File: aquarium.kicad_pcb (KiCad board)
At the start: 2 copper layers, 104 x 47 mm, 40 parts, among them U1 MOC3063, U2 MOC3063

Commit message: ATmega48PA changet to ATmega8A
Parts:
- DD4: value ATMEGA48PA -> ATMEGA8A
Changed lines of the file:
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@@
     (links 93)
     (no_connects 2)
-    (area 74.899999 67.875 220.208334 135.300002)
+    (area 92.924999 82.924999 197.075001 130.075001)
     (thickness 1.6)
     (drawings 50)
@@
       (effects (font (size 1 1) (thickness 0.15)))
     )
-    (fp_text value ATMEGA48PA (at 0 0 90) (layer F.SilkS) hide
-      (effects (font (size 1 1) (thickness 0.15)))
-    )
+    (fp_text value ATMEGA8A (at 0 0 90) (layer F.SilkS) hide
+      (effects (font (size 1 1) (thickness 0.15)))
+    )

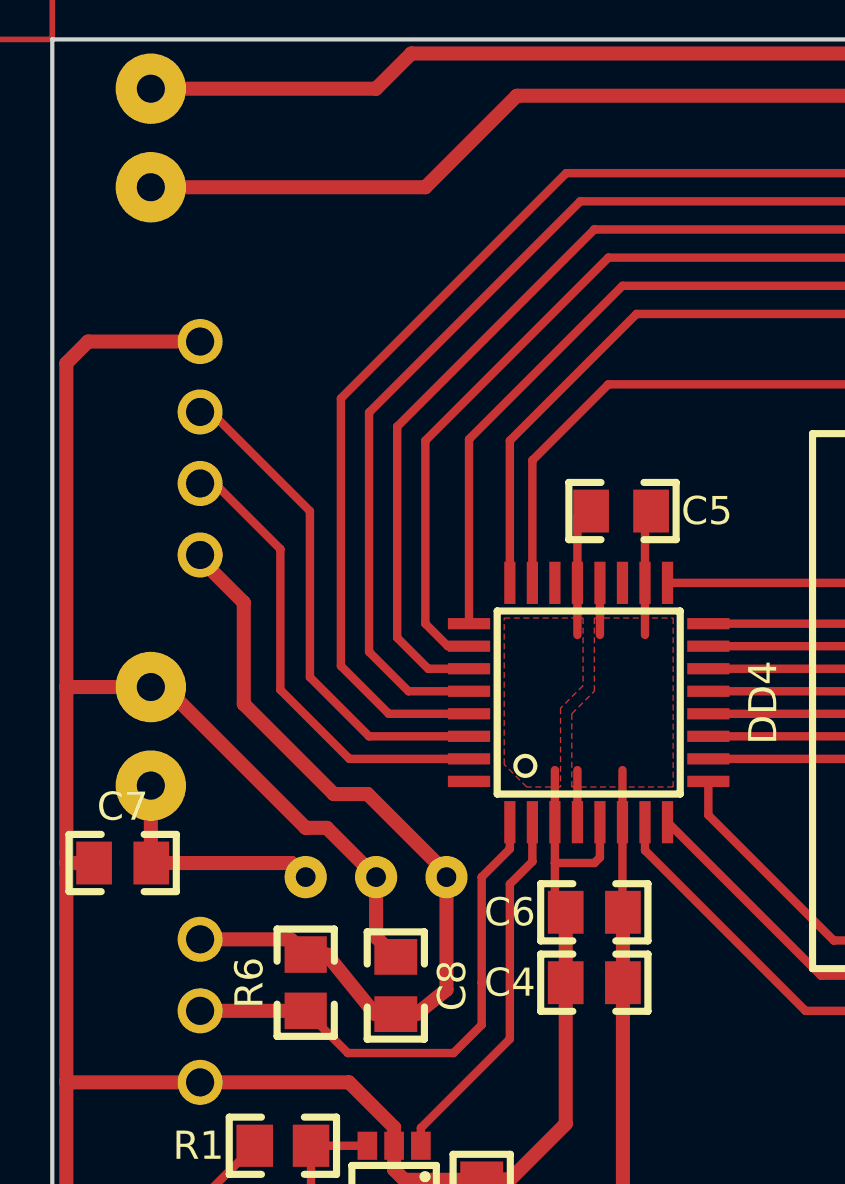
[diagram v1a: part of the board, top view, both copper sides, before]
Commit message: Corrected sensitivity of the sensor and added noise protection on Reset pin.
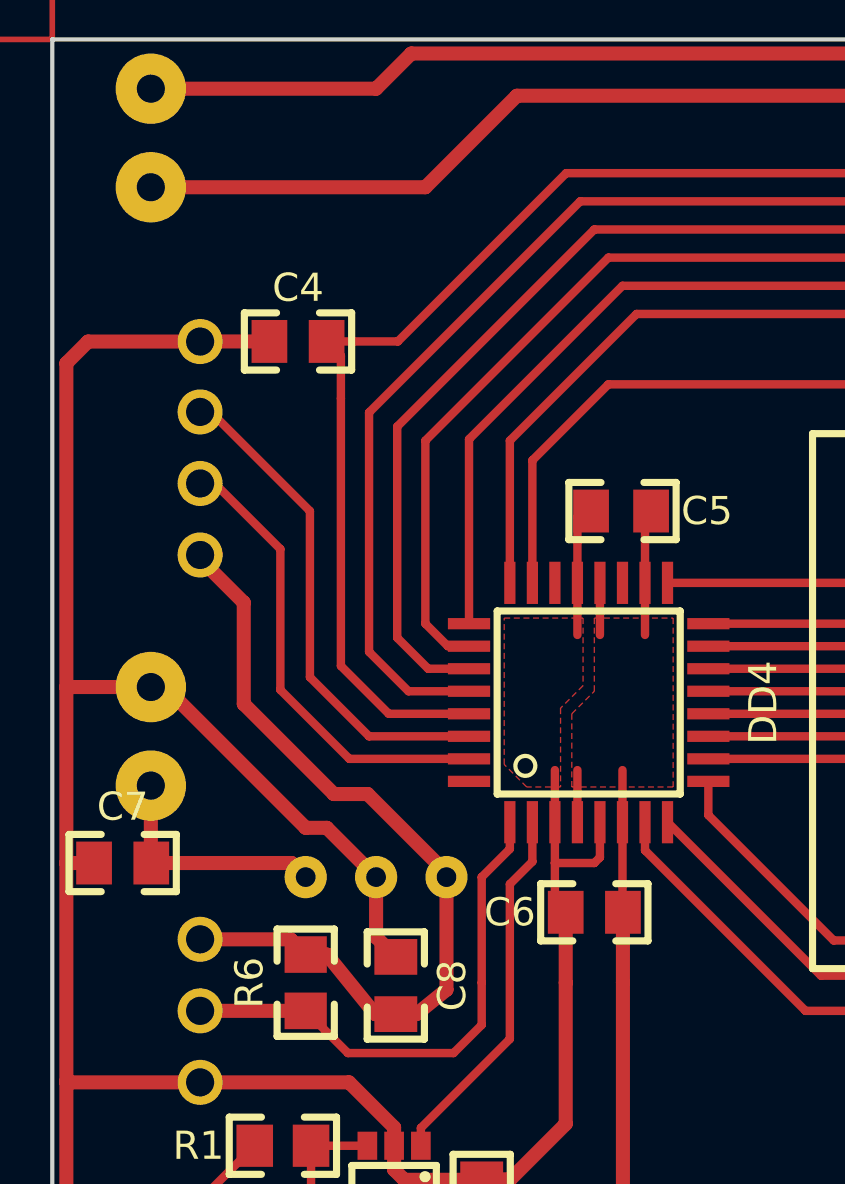
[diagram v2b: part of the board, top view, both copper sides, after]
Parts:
- C2: value 0.01 -> 2n2
- R1: value 22k -> 100k
- moved C4 25.1 mm to (101.7, 93.7)
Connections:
- C4 pad 1: +5B -> /~RESET
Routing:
- net GND: track 244.3 -> 246.7 mm
- net /~RESET: track 96.4 -> 98.3 mm
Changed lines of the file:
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@@
-(kicad_pcb (version 4) (host pcbnew "(2015-12-27 BZR 5198)-new_icons")
+(kicad_pcb (version 4) (host pcbnew "(2016-01-20 BZR 5201)-new_icons")
   (general
     (links 93)
@@
     (thickness 1.6)
     (drawings 50)
-    (tracks 297)
+    (tracks 302)
     (zones 0)
     (modules 40)
@@
   )
   (setup
-    (last_trace_width 0.25)
+    (last_trace_width 0.5)
     (user_trace_width 0.2)
     (user_trace_width 0.3)
@@
       (effects (font (size 1 1) (thickness 0.15)))
     )
-    (fp_text value 0.01 (at 0 0 90) (layer F.SilkS) hide
+    (fp_text value 2n2 (at 0 0 90) (layer F.SilkS) hide
       (effects (font (size 1 1) (thickness 0.15)))
     )
@@
   )
   (module Конденсаторы:SMD_0805 (layer F.Cu)
-    (at 112.25 116.5)
+    (at 101.727 93.726)
     (descr "Capacitor smd 0805")
     (tags C)
-    (fp_text reference C4 (at -3 0) (layer F.SilkS)
+    (fp_text reference C4 (at 0 -1.905) (layer F.SilkS)
       (effects (font (size 1 1) (thickness 0.15)))
     )
@@
     (fp_line (start -1.905 1.016) (end -0.762 1.016) (layer F.SilkS) (width 0.254))
     (pad 1 smd rect (at 1.016 0) (size 1.27 1.524) (layers F.Cu F.Paste F.Mask)
-      (net 2 +5B))
+      (net 30 /~RESET))
     (pad 2 smd rect (at -1.016 0) (size 1.27 1.524) (layers F.Cu F.Paste F.Mask)
       (net 1 GND))
@@
       (effects (font (size 1 1) (thickness 0.15)))
     )
-    (fp_text value 22k (at 0 0 180) (layer F.SilkS) hide
+    (fp_text value 100k (at 0 0 180) (layer F.SilkS) hide
       (effects (font (size 1 1) (thickness 0.15)))
     )
@@
   (segment (start 197 83) (end 197 78) (width 0.2) (layer F.Cu) (net 0))
   (segment (start 197 83) (end 202 83) (width 0.2) (layer F.Cu) (net 0))
+  (segment (start 100.711 93.726) (end 98.254 93.726) (width 0.5) (layer F.Cu) (net 1) (status C00000))
+  (segment (start 98.254 93.726) (end 98.25 93.73) (width 0.3) (layer F.Cu) (net 1) (status C00000))
   (segment (start 104.5 112.75) (end 104.5 114.884) (width 0.5) (layer F.Cu) (net 1))
   (segment (start 104.5 114.884) (end 105.2 115.584) (width 0.5) (layer F.Cu) (net 1))
@@
   (segment (start 113.266 114) (end 113.266 116.5) (width 0.5) (layer F.Cu) (net 2) (status 30))
   (segment (start 108.25 125.516) (end 113.266 125.516) (width 0.5) (layer F.Cu) (net 2) (status 10))
-  (segment (start 113.266 125.516) (end 113.266 116.5) (width 0.5) (layer F.Cu) (net 2) (status 20))
   (segment (start 113.25 110.8) (end 113.25 113.984) (width 0.3) (layer F.Cu) (net 2) (status 30))
   (segment (start 113.25 113.984) (end 113.266 114) (width 0.3) (layer F.Cu) (net 2) (status 30))
@@
   (segment (start 114 99.868) (end 113.882 99.75) (width 0.3) (layer F.Cu) (net 2) (status 30))
   (segment (start 98.25 101.31) (end 98.81 101.31) (width 0.5) (layer F.Cu) (net 2) (status 30))
+  (segment (start 113.266 125.516) (end 113.266 116.5) (width 0.5) (layer F.Cu) (net 2) (status 20))
   (segment (start 151.35 116.66) (end 151.35 112.05) (width 0.3) (layer F.Cu) (net 3) (status 30))
   (segment (start 151.35 112.05) (end 151.4 112) (width 0.3) (layer F.Cu) (net 3) (status 30))
@@
   (segment (start 120.3 116.25) (end 114.85 110.8) (width 0.3) (layer F.Cu) (net 29))
   (segment (start 129.25 116.25) (end 120.3 116.25) (width 0.3) (layer F.Cu) (net 29))
+  (segment (start 103.25 95.75) (end 103.25 94.233) (width 0.3) (layer F.Cu) (net 30) (status 800000))
+  (segment (start 103.25 94.233) (end 102.743 93.726) (width 0.3) (layer F.Cu) (net 30) (status 800000))
+  (segment (start 102.743 93.726) (end 105.274 93.726) (width 0.3) (layer F.Cu) (net 30) (status 400000))
   (segment (start 107.8 106.95) (end 104.95 106.95) (width 0.3) (layer F.Cu) (net 30) (status 10))
   (segment (start 160.77 94.75) (end 159.79 95.73) (width 0.3) (layer F.Cu) (net 30) (status 20))
@@
   (segment (start 165.25 87.75) (end 168 90.5) (width 0.3) (layer F.Cu) (net 30))
   (segment (start 111.25 87.75) (end 165.25 87.75) (width 0.3) (layer F.Cu) (net 30))
-  (segment (start 103.25 95.75) (end 111.25 87.75) (width 0.3) (layer F.Cu) (net 30))
+  (segment (start 105.274 93.726) (end 111.25 87.75) (width 0.3) (layer F.Cu) (net 30))
   (segment (start 103.25 105.25) (end 103.25 95.75) (width 0.3) (layer F.Cu) (net 30))
   (segment (start 104.95 106.95) (end 103.25 105.25) (width 0.3) (layer F.Cu) (net 30))
